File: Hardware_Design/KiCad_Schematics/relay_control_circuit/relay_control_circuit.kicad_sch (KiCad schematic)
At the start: 6 parts, among them J1 Screw_Terminal_01x02, K2 SANYOU_SRD_Form_C, SW1 SW_Push

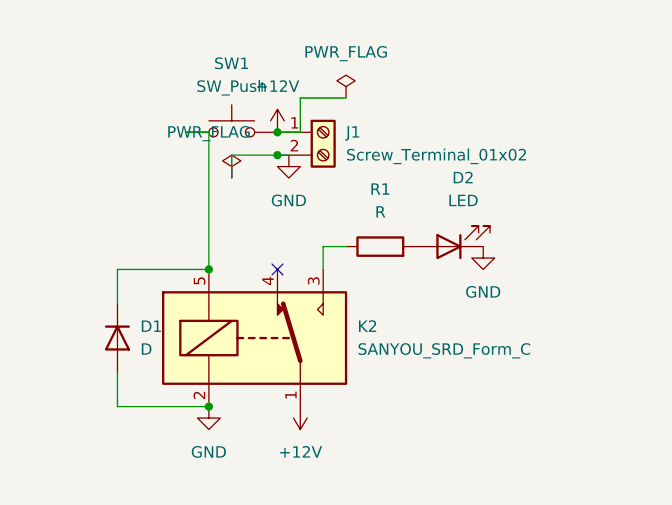
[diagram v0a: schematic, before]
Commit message: Add README and clean up schematic for Relay Control Circuit
Added the README.md file for the Relay Control Circuit project. Refactored the schematic and PCB layout to be cleaner and more visually appealing by reducing unnecessary screw terminals into a single block, simplifying the overall design.
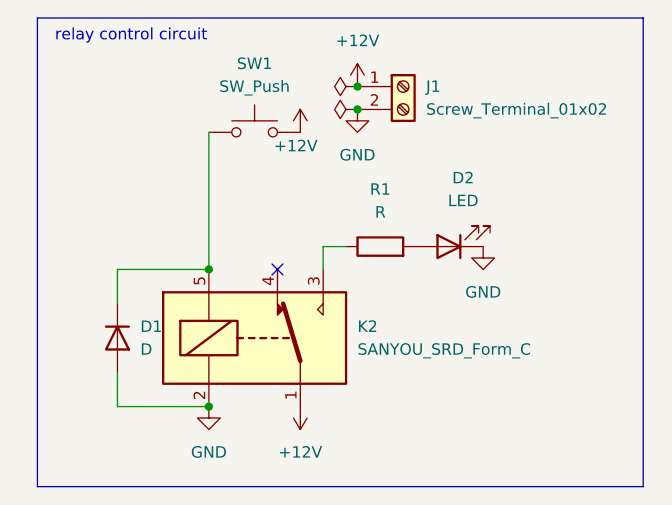
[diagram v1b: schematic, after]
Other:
- note added: "relay control circuit"
- moved on the sheet: SW1
